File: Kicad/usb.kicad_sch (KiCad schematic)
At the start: 28 parts, among them J901 USB Ports External, J902 USB Ports Internal, U901 AP2501, U902 XR22404CG28, U903 MIC2005A-2YM5, U904 MIC2005A-2YM5, U905 MIC2005A-2YM5, U906 MIC2005A-2YM5, Y901 12M

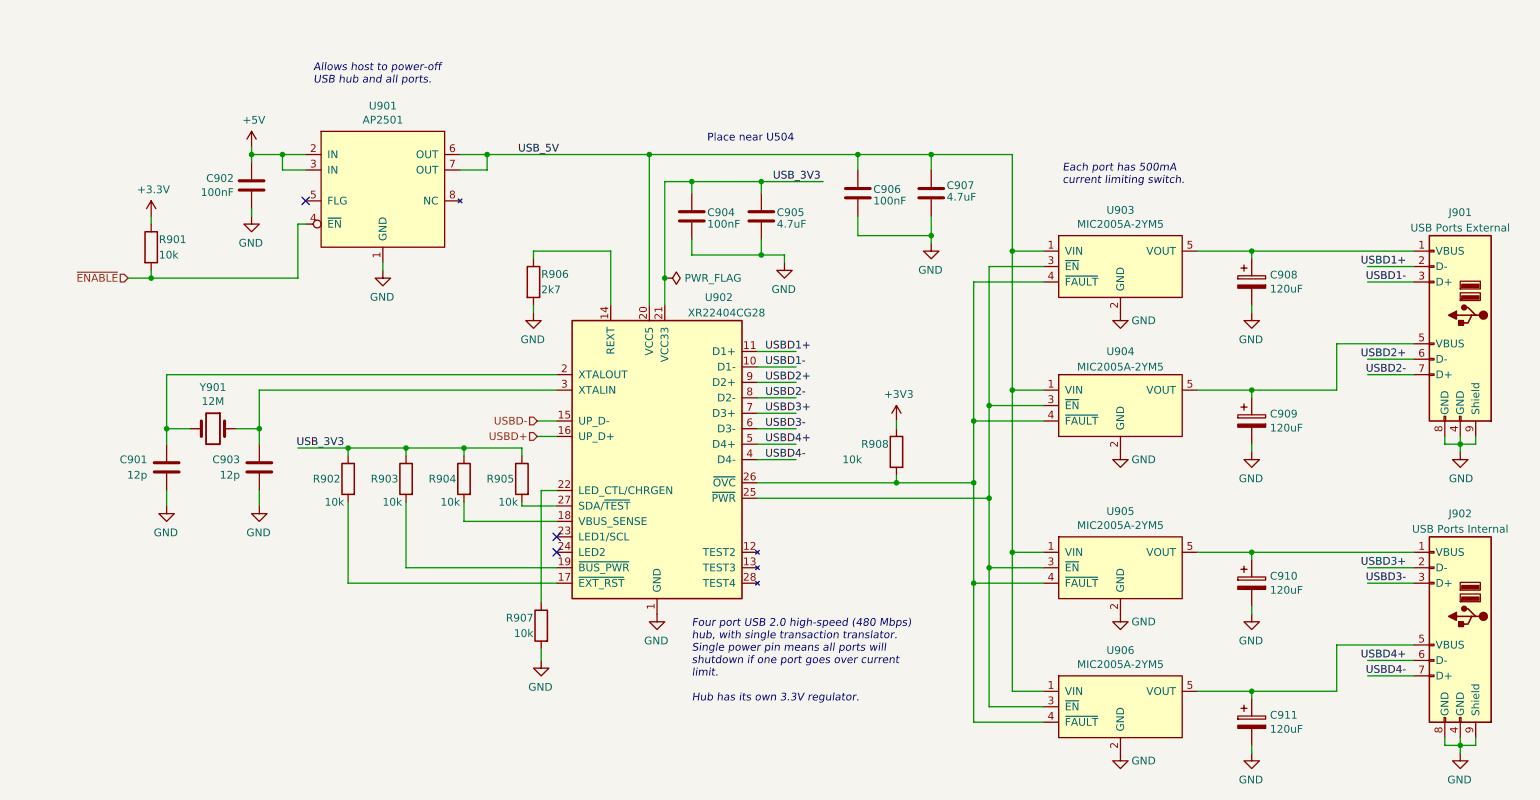
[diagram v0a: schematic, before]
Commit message: Update schematic files to Kicad 6.
Had to fix some symbols which didn't have perfect matches in K6.
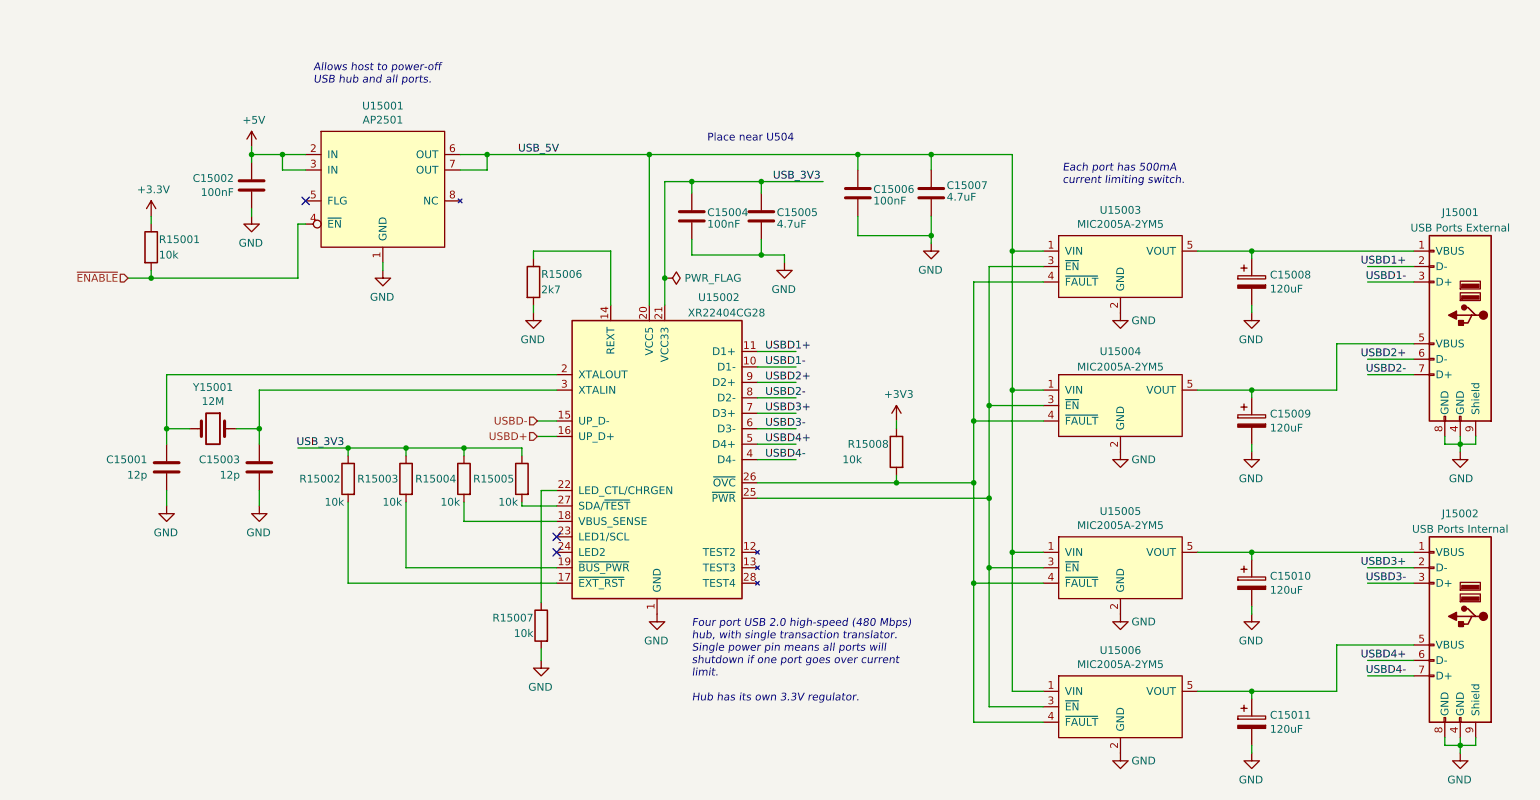
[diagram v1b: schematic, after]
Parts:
- C15008: renamed from C908; symbol Neotron-Common-Hardware-rescue:CP-Device -> Device:C_Polarized
- C15009: renamed from C909; symbol Neotron-Common-Hardware-rescue:CP-Device -> Device:C_Polarized
- C15010: renamed from C910; symbol Neotron-Common-Hardware-rescue:CP-Device -> Device:C_Polarized
- C15011: renamed from C911; symbol Neotron-Common-Hardware-rescue:CP-Device -> Device:C_Polarized
- renumbered C901 to C15001, C902 to C15002, C903 to C15003, C904 to C15004, C905 to C15005, C906 to C15006, C907 to C15007, J901 to J15001, J902 to J15002, R901 to R15001, R902 to R15002, R903 to R15003, R904 to R15004, R905 to R15005, R906 to R15006, R907 to R15007, R908 to R15008, U901 to U15001, U902 to U15002, U903 to U15003, U904 to U15004, U905 to U15005, U906 to U15006, Y901 to Y15001
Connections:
- net +3V3: no longer R15001.1
- new net +3.3V: R15001.1

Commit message: Imported sheets from Neotron Pico.
Standardised on +3V3 not +3.3V
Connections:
- net +3.3V is gone; now on net +3V3: R15001.1
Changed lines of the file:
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@@
     (pin "2")
   )
-  (symbol (lib_id "power:+3.3V") (at 36.83 48.26 0) (unit 1)
+  (symbol (lib_id "power:+3V3") (at 36.83 48.26 0) (unit 1)
     (in_bom yes) (on_board yes)
     (property "Reference" "#PWR015001" (id 0) (at 36.83 52.07 0)

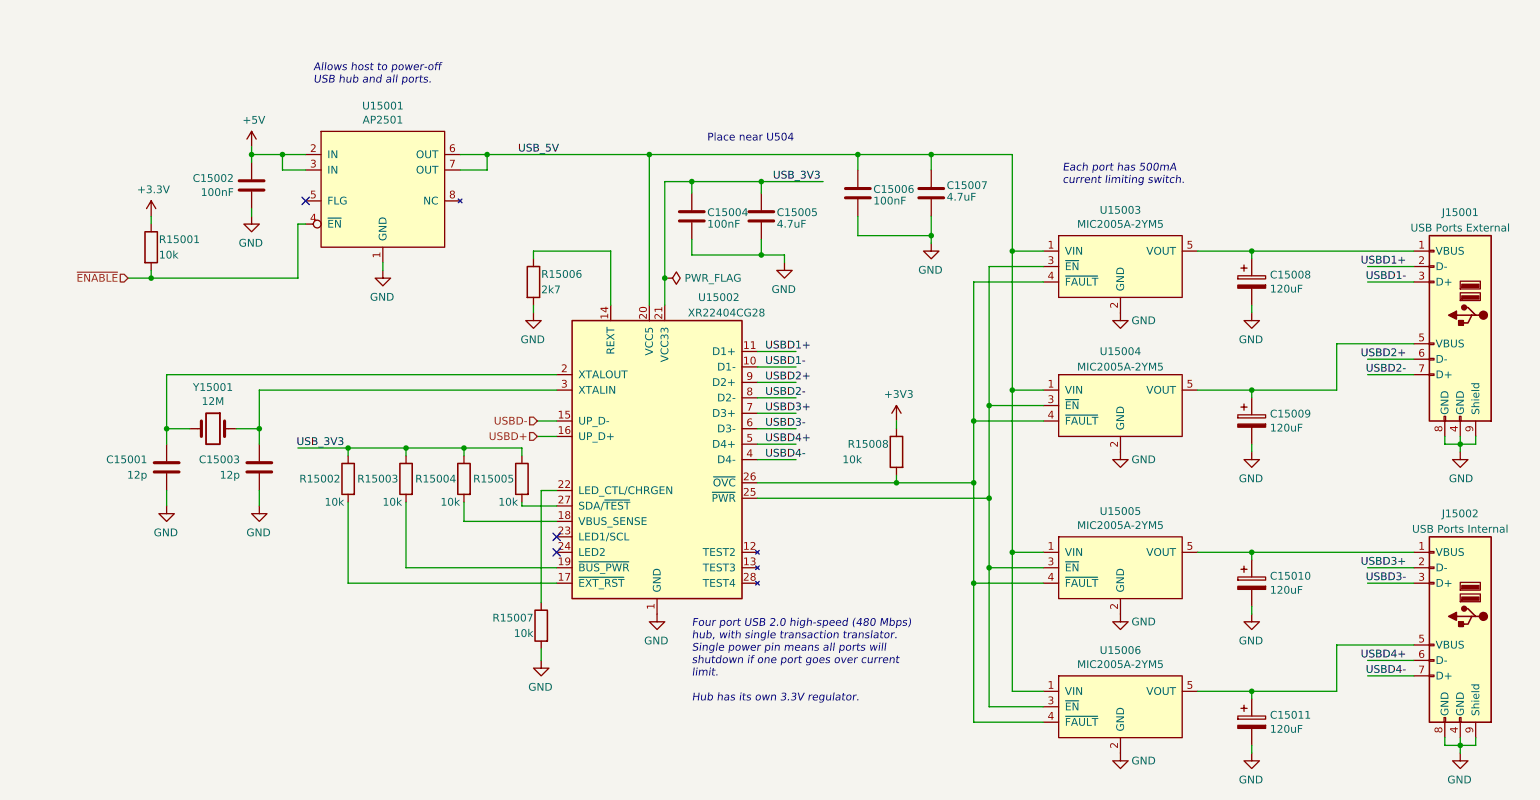
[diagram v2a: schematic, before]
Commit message: Set missing footprints and update PCB
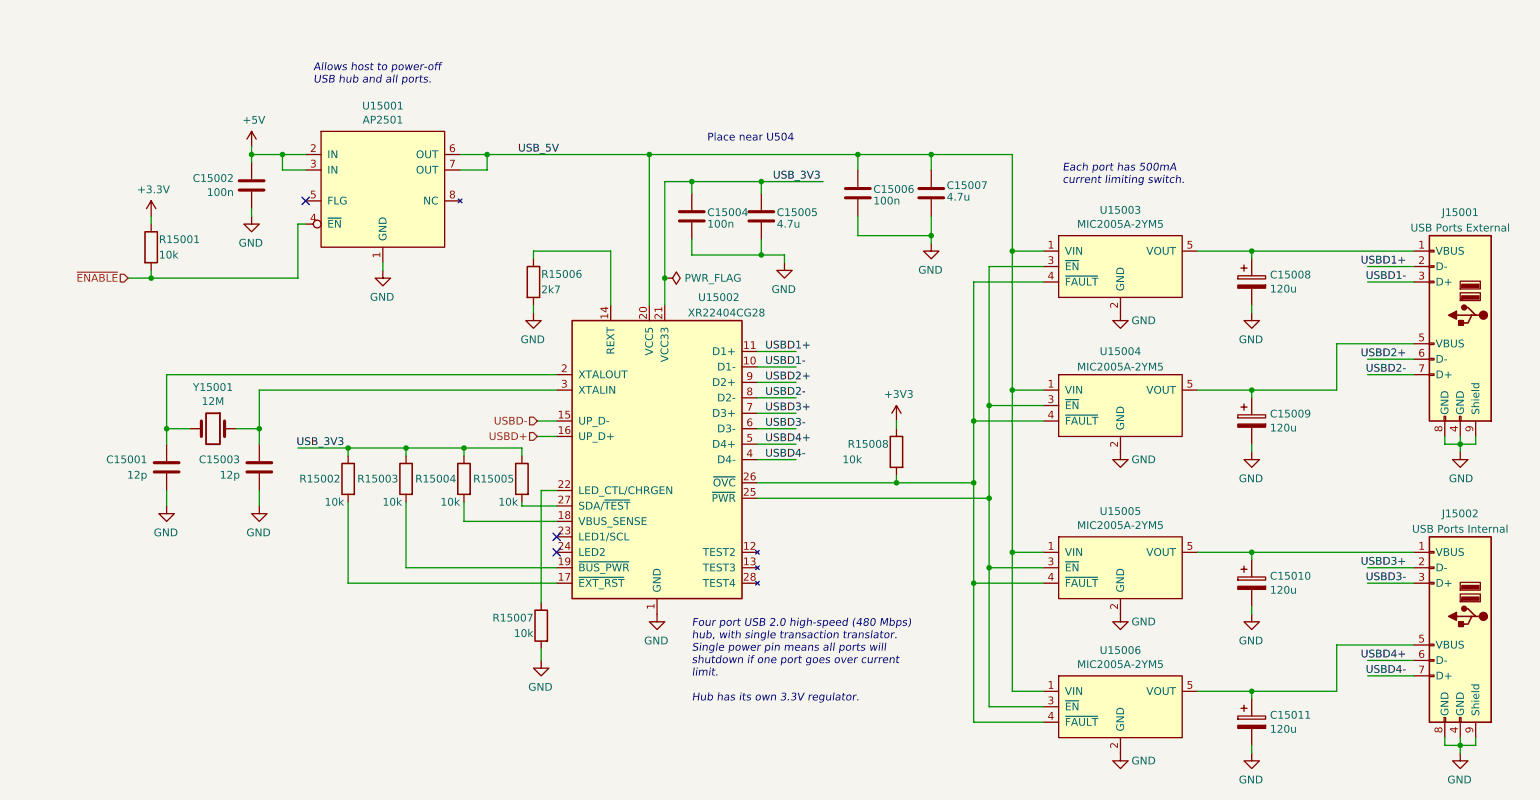
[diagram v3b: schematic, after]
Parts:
- C15002, C15004, C15006: value 100nF -> 100n; Digikey BC1150CT-ND -> (none); JLCPCB Collection (none) -> Basic; LCSC Part# (none) -> C49678; MPN CPL-CAP-X7R-0805-100NF-50V -> CC0805KRX7R9BB104
- C15005: value 4.7uF -> 4.7u; Digikey 1276-6464-1-ND -> (none); MPN CPL-CAP-X5R-0805-4.7UF-25V -> (none); Manufacturer Samsung -> (none)
- C15007: value 4.7uF -> 4.7u; Digikey 1276-1065-1-ND -> (none); MPN CPL-CAP-X5R-0805-4.7UF-25V -> (none); Manufacturer Samsung -> (none)
- C15008, C15009, C15010, C15011: value 120uF -> 120u
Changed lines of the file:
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@@
       (effects (font (size 1.27 1.27)) (justify left))
     )
-    (property "Value" "4.7uF" (id 1) (at 167.64 45.085 0)
+    (property "Value" "4.7u" (id 1) (at 167.64 45.085 0)
       (effects (font (size 1.27 1.27)) (justify left))
     )
@@
       (effects (font (size 1.27 1.27)) hide)
     )
-    (property "Digikey" "1276-1065-1-ND" (id 5) (at 165.1 44.45 0)
-      (effects (font (size 1.27 1.27)) hide)
-    )
-    (property "MPN" "CPL-CAP-X5R-0805-4.7UF-25V" (id 6) (at 165.1 44.45 0)
-      (effects (font (size 1.27 1.27)) hide)
-    )
-    (property "Manufacturer" "Samsung" (id 7) (at 165.1 44.45 0)
+    (property "Digikey" "" (id 5) (at 165.1 44.45 0)
+      (effects (font (size 1.27 1.27)) hide)
+    )
+    (property "MPN" "" (id 6) (at 165.1 44.45 0)
+      (effects (font (size 1.27 1.27)) hide)
+    )
+    (property "Manufacturer" "" (id 7) (at 165.1 44.45 0)
       (effects (font (size 1.27 1.27)) hide)
     )
@@
       (effects (font (size 1.27 1.27)) (justify left))
     )
-    (property "Value" "100nF" (id 1) (at 155.575 45.72 0)
+    (property "Value" "100n" (id 1) (at 155.575 45.72 0)
       (effects (font (size 1.27 1.27)) (justify left))
     )
@@
       (effects (font (size 1.27 1.27)) hide)
     )
-    (property "Digikey" "BC1150CT-ND" (id 5) (at 153.035 44.45 0)
-      (effects (font (size 1.27 1.27)) hide)
-    )
-    (property "MPN" "CPL-CAP-X7R-0805-100NF-50V" (id 6) (at 153.035 44.45 0)
+    (property "Digikey" "~" (id 5) (at 153.035 44.45 0)
+      (effects (font (size 1.27 1.27)) hide)
+    )
+    (property "MPN" "CC0805KRX7R9BB104" (id 6) (at 153.035 44.45 0)
       (effects (font (size 1.27 1.27)) hide)
     )
@@
     )
     (property "Voltage" "16V" (id 10) (at 153.035 44.45 0)
+      (effects (font (size 1.27 1.27)) hide)
+    )
+    (property "JLCPCB Collection" "Basic" (id 11) (at 153.035 44.45 0)
+      (effects (font (size 1.27 1.27)) hide)
+    )
+    (property "LCSC Part#" "C49678" (id 12) (at 153.035 44.45 0)
       (effects (font (size 1.27 1.27)) hide)
     )
@@
       (effects (font (size 1.27 1.27)) (justify left))
     )
-    (property "Value" "4.7uF" (id 1) (at 139.7 49.53 0)
+    (property "Value" "4.7u" (id 1) (at 139.7 49.53 0)
       (effects (font (size 1.27 1.27)) (justify left))
     )
@@
       (effects (font (size 1.27 1.27)) hide)
     )
-    (property "Digikey" "1276-6464-1-ND" (id 5) (at 137.16 48.26 0)
-      (effects (font (size 1.27 1.27)) hide)
-    )
-    (property "MPN" "CPL-CAP-X5R-0805-4.7UF-25V" (id 6) (at 137.16 48.26 0)
-      (effects (font (size 1.27 1.27)) hide)
-    )
-    (property "Manufacturer" "Samsung" (id 7) (at 137.16 48.26 0)
+    (property "Digikey" "" (id 5) (at 137.16 48.26 0)
+      (effects (font (size 1.27 1.27)) hide)
+    )
+    (property "MPN" "" (id 6) (at 137.16 48.26 0)
+      (effects (font (size 1.27 1.27)) hide)
+    )
+    (property "Manufacturer" "" (id 7) (at 137.16 48.26 0)
       (effects (font (size 1.27 1.27)) hide)
     )
@@
       (effects (font (size 1.27 1.27)) (justify left))
     )
-    (property "Value" "120uF" (id 1) (at 220.8022 60.198 0)
+    (property "Value" "120u" (id 1) (at 220.8022 60.198 0)
       (effects (font (size 1.27 1.27)) (justify left))
     )
@@
       (effects (font (size 1.27 1.27)) (justify left))
     )
-    (property "Value" "120uF" (id 1) (at 220.8022 83.058 0)
+    (property "Value" "120u" (id 1) (at 220.8022 83.058 0)
       (effects (font (size 1.27 1.27)) (justify left))
     )
@@
       (effects (font (size 1.27 1.27)) (justify left))
     )
-    (property "Value" "120uF" (id 1) (at 220.8022 109.728 0)
+    (property "Value" "120u" (id 1) (at 220.8022 109.728 0)
       (effects (font (size 1.27 1.27)) (justify left))
     )
@@
       (effects (font (size 1.27 1.27)) (justify left))
     )
-    (property "Value" "120uF" (id 1) (at 220.8022 132.588 0)
+    (property "Value" "120u" (id 1) (at 220.8022 132.588 0)
       (effects (font (size 1.27 1.27)) (justify left))
     )
@@
       (effects (font (size 1.27 1.27)) (justify left))
     )
-    (property "Value" "100nF" (id 1) (at 50.419 44.323 0)
+    (property "Value" "100n" (id 1) (at 50.419 44.323 0)
       (effects (font (size 1.27 1.27)) (justify left))
     )
@@
       (effects (font (size 1.27 1.27)) hide)
     )
-    (property "Digikey" "BC1150CT-ND" (id 5) (at 53.34 43.18 0)
-      (effects (font (size 1.27 1.27)) hide)
-    )
-    (property "MPN" "CPL-CAP-X7R-0805-100NF-50V" (id 6) (at 53.34 43.18 0)
+    (property "Digikey" "~" (id 5) (at 53.34 43.18 0)
+      (effects (font (size 1.27 1.27)) hide)
+    )
+    (property "MPN" "CC0805KRX7R9BB104" (id 6) (at 53.34 43.18 0)
       (effects (font (size 1.27 1.27)) hide)
     )
@@
     )
     (property "Voltage" "16V" (id 10) (at 53.34 43.18 0)
+      (effects (font (size 1.27 1.27)) hide)
+    )
+    (property "JLCPCB Collection" "Basic" (id 11) (at 53.34 43.18 0)
+      (effects (font (size 1.27 1.27)) hide)
+    )
+    (property "LCSC Part#" "C49678" (id 12) (at 53.34 43.18 0)
       (effects (font (size 1.27 1.27)) hide)
     )
@@
       (effects (font (size 1.27 1.27)) (justify left))
     )
-    (property "Value" "100nF" (id 1) (at 128.27 49.53 0)
+    (property "Value" "100n" (id 1) (at 128.27 49.53 0)
       (effects (font (size 1.27 1.27)) (justify left))
     )
@@
       (effects (font (size 1.27 1.27)) hide)
     )
-    (property "Digikey" "BC1150CT-ND" (id 5) (at 125.73 48.26 0)
-      (effects (font (size 1.27 1.27)) hide)
-    )
-    (property "MPN" "CPL-CAP-X7R-0805-100NF-50V" (id 6) (at 125.73 48.26 0)
+    (property "Digikey" "~" (id 5) (at 125.73 48.26 0)
+      (effects (font (size 1.27 1.27)) hide)
+    )
+    (property "MPN" "CC0805KRX7R9BB104" (id 6) (at 125.73 48.26 0)
       (effects (font (size 1.27 1.27)) hide)
     )
@@
       (effects (font (size 1.27 1.27)) hide)
     )
+    (property "JLCPCB Collection" "Basic" (id 11) (at 125.73 48.26 0)
+      (effects (font (size 1.27 1.27)) hide)
+    )
+    (property "LCSC Part#" "C49678" (id 12) (at 125.73 48.26 0)
+      (effects (font (size 1.27 1.27)) hide)
+    )

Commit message: Re-imported from Neotron Pico v1.1.
This time I deleted the sheets from the top level and then re-added pointing at the new files. I also reset the PCB dimensions to match the Neotron Pico.

This seems to have done a better job importing footprints.
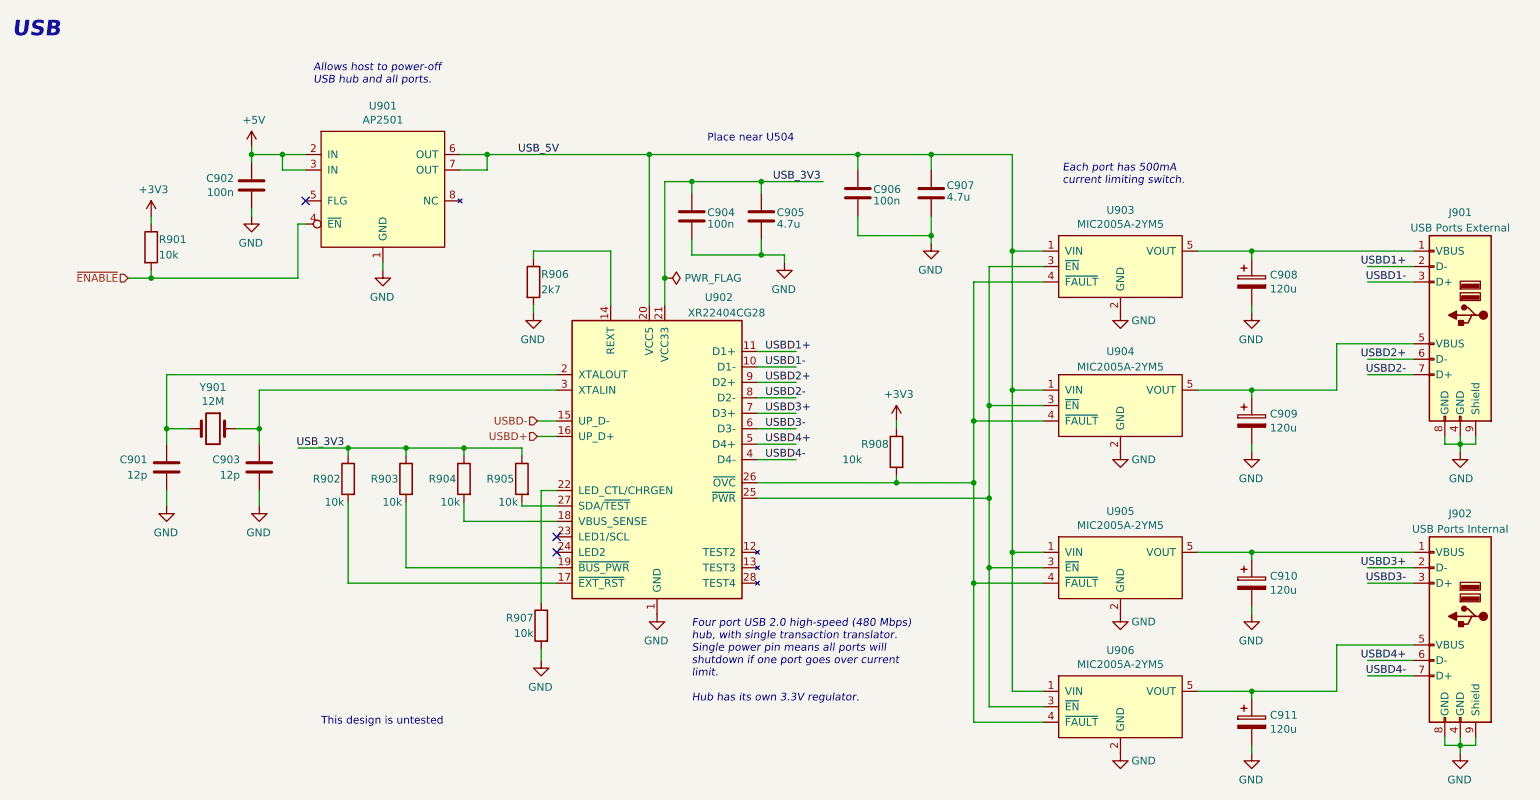
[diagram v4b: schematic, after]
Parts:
- renumbered C15001 to C901, C15002 to C902, C15003 to C903, C15004 to C904, C15005 to C905, C15006 to C906, C15007 to C907, C15008 to C908, C15009 to C909, C15010 to C910, C15011 to C911, J15001 to J901, J15002 to J902, R15001 to R901, R15002 to R902, R15003 to R903, R15004 to R904, R15005 to R905, R15006 to R906, R15007 to R907, R15008 to R908, U15001 to U901, U15002 to U902, U15003 to U903, U15004 to U904, U15005 to U905, U15006 to U906, Y15001 to Y901
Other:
- note added: "This design is untested"
- note added: "USB"
